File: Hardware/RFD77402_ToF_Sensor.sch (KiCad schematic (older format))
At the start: 18 parts, among them J1 QWIIC_CONNECTORJS-1MM, J2 QWIIC_CONNECTORJS-1MM, J3 CONN_01, J4 I2C_STANDARD, U1 RFD77402, U4 CC_LICENSE

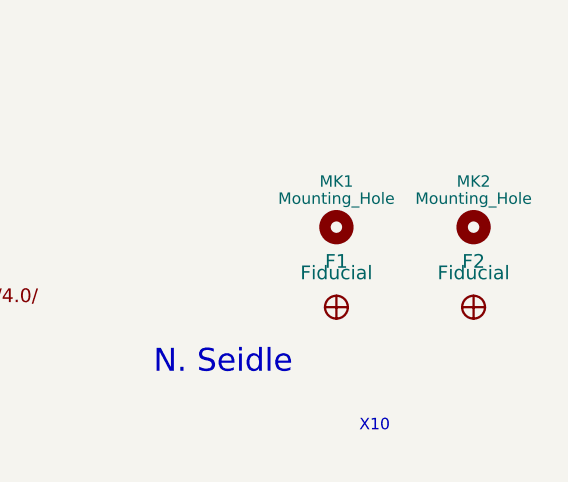
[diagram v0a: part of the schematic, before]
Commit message: Added fiducials
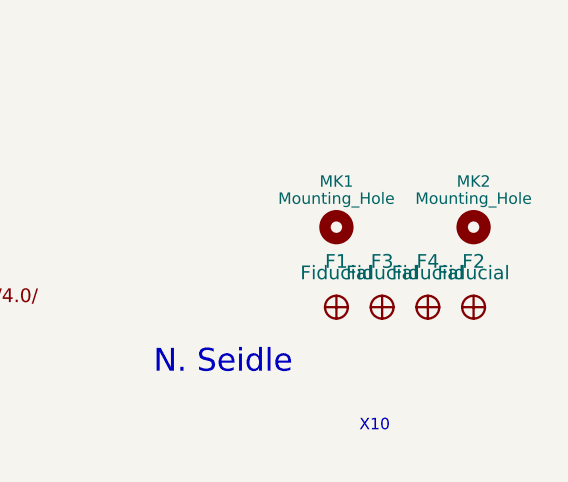
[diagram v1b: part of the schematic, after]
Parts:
- added F3, F4: Fiducial, Aesthetics:FIDUCIAL-MICRO, symbol Fiducial
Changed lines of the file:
@@
 $EndComp
 $Comp
-L GND #PWR01
+L GND #PWR8
 U 1 1 5907663F
 P 4650 5450
-F 0 "#PWR01" H 4650 5200 50  0001 C CNN
+F 0 "#PWR8" H 4650 5200 50  0001 C CNN
 F 1 "GND" H 4650 5300 50  0000 C CNN
 F 2 "" H 4650 5450 50  0001 C CNN
@@
 $EndComp
 $Comp
-L GND #PWR02
+L GND #PWR10
 U 1 1 5907732D
 P 4950 3200
-F 0 "#PWR02" H 4950 2950 50  0001 C CNN
+F 0 "#PWR10" H 4950 2950 50  0001 C CNN
 F 1 "GND" H 4950 3050 50  0000 C CNN
 F 2 "" H 4950 3200 50  0001 C CNN
@@
 $EndComp
 $Comp
-L GND #PWR03
+L GND #PWR4
 U 1 1 59077368
 P 4450 3200
-F 0 "#PWR03" H 4450 2950 50  0001 C CNN
+F 0 "#PWR4" H 4450 2950 50  0001 C CNN
 F 1 "GND" H 4450 3050 50  0000 C CNN
 F 2 "" H 4450 3200 50  0001 C CNN
@@
 $EndComp
 $Comp
-L +3.3V #PWR04
+L +3.3V #PWR3
 U 1 1 59078478
 P 4450 2650
-F 0 "#PWR04" H 4450 2500 50  0001 C CNN
+F 0 "#PWR3" H 4450 2500 50  0001 C CNN
 F 1 "+3.3V" H 4450 2790 50  0000 C CNN
 F 2 "" H 4450 2650 50  0001 C CNN
@@
 $EndComp
 $Comp
-L +3.3V #PWR05
+L +3.3V #PWR9
 U 1 1 590784B0
 P 4950 2700
-F 0 "#PWR05" H 4950 2550 50  0001 C CNN
+F 0 "#PWR9" H 4950 2550 50  0001 C CNN
 F 1 "+3.3V" H 4950 2840 50  0000 C CNN
 F 2 "" H 4950 2700 50  0001 C CNN
@@
 $EndComp
 $Comp
-L +3.3V #PWR06
+L +3.3V #PWR5
 U 1 1 590784E8
 P 4650 4000
-F 0 "#PWR06" H 4650 3850 50  0001 C CNN
+F 0 "#PWR5" H 4650 3850 50  0001 C CNN
 F 1 "+3.3V" H 4650 4140 50  0000 C CNN
 F 2 "" H 4650 4000 50  0001 C CNN
@@
 $EndComp
 $Comp
-L +3.3V #PWR07
+L +3.3V #PWR11
 U 1 1 59078610
 P 5850 4000
-F 0 "#PWR07" H 5850 3850 50  0001 C CNN
+F 0 "#PWR11" H 5850 3850 50  0001 C CNN
 F 1 "+3.3V" H 5850 4140 50  0000 C CNN
 F 2 "" H 5850 4000 50  0001 C CNN
@@
 $EndComp
 $Comp
-L +3.3V #PWR08
+L +3.3V #PWR7
 U 1 1 59078648
 P 4650 4950
-F 0 "#PWR08" H 4650 4800 50  0001 C CNN
+F 0 "#PWR7" H 4650 4800 50  0001 C CNN
 F 1 "+3.3V" H 4650 5090 50  0000 C CNN
 F 2 "" H 4650 4950 50  0001 C CNN
@@
 $EndComp
 $Comp
-L GND #PWR09
+L GND #PWR12
 U 1 1 590793B0
 P 5850 4500
-F 0 "#PWR09" H 5850 4250 50  0001 C CNN
+F 0 "#PWR12" H 5850 4250 50  0001 C CNN
 F 1 "GND" H 5850 4350 50  0000 C CNN
 F 2 "" H 5850 4500 50  0001 C CNN
@@
 $EndComp
 $Comp
-L GND #PWR010
+L GND #PWR6
 U 1 1 590795D3
 P 4650 4500
-F 0 "#PWR010" H 4650 4250 50  0001 C CNN
+F 0 "#PWR6" H 4650 4250 50  0001 C CNN
 F 1 "GND" H 4650 4350 50  0000 C CNN
 F 2 "" H 4650 4500 50  0001 C CNN
@@
 	5850 3100 5950 3100
 $Comp
-L +3.3V #PWR011
+L +3.3V #PWR13
 U 1 1 5907C92A
 P 6200 1950
-F 0 "#PWR011" H 6200 1800 50  0001 C CNN
+F 0 "#PWR13" H 6200 1800 50  0001 C CNN
 F 1 "+3.3V" H 6200 2090 50  0000 C CNN
 F 2 "" H 6200 1950 50  0001 C CNN
@@
 Connection ~ 4950 2800
 $Comp
-L +3.3V #PWR012
+L +3.3V #PWR1
 U 1 1 591D2B23
 P 4150 2650
-F 0 "#PWR012" H 4150 2500 50  0001 C CNN
+F 0 "#PWR1" H 4150 2500 50  0001 C CNN
 F 1 "+3.3V" H 4150 2790 50  0000 C CNN
 F 2 "" H 4150 2650 50  0001 C CNN
@@
 $EndComp
 $Comp
-L GND #PWR013
+L GND #PWR2
 U 1 1 591D2B5E
 P 4150 3200
-F 0 "#PWR013" H 4150 2950 50  0001 C CNN
+F 0 "#PWR2" H 4150 2950 50  0001 C CNN
 F 1 "GND" H 4150 3050 50  0000 C CNN
 F 2 "" H 4150 3200 50  0001 C CNN
@@
 	1    0    0    -1
 $EndComp
+$Comp
+L Fiducial F3
+U 1 1 5A0F19BD
+P 10000 7300
+F 0 "F3" H 10000 7500 60  0000 C CNN
+F 1 "Fiducial" H 10000 7450 60  0000 C CNN
+F 2 "Aesthetics:FIDUCIAL-MICRO" H 10000 7300 60  0001 C CNN
+F 3 "" H 10000 7300 60  0001 C CNN
+	1    10000 7300
+	1    0    0    -1
+$EndComp
+$Comp
+L Fiducial F4
+U 1 1 5A0F1A01
+P 10200 7300
+F 0 "F4" H 10200 7500 60  0000 C CNN
+F 1 "Fiducial" H 10200 7450 60  0000 C CNN
+F 2 "Aesthetics:FIDUCIAL-MICRO" H 10200 7300 60  0001 C CNN
+F 3 "" H 10200 7300 60  0001 C CNN
+	1    10200 7300
+	1    0    0    -1
+$EndComp

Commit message: Post design review changes
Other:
- note added: "Distance Sensor"
- note added: "I2C Address: 0X4C"
- note added: "I2C Connections"
- note added: "Jumper connects the I2C pullup resistors.\nDisconnect to use your own resistors."
- note added: "v01"
- note removed: "X10"
- moved on the sheet: F1, F2, F3, F4, MK1, MK2
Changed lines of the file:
@@
 N. Seidle
 Text Notes 9900 7850 0    50   ~ 0
-X10
-Wire Wire Line
-	5050 2800 4950 2800
-Wire Wire Line
-	4950 2700 4950 2900
-Wire Wire Line
-	4450 2650 4450 2800
-Wire Wire Line
-	4650 4300 4650 4000
-Wire Wire Line
-	5600 4300 5850 4300
-Wire Wire Line
-	5850 4300 5850 4000
-Wire Wire Line
-	4300 5250 4650 5250
-Wire Wire Line
-	4650 5250 4650 4950
-Wire Wire Line
-	5050 3100 4950 3100
-Wire Wire Line
-	4950 3000 4950 3200
-Wire Wire Line
-	4450 3100 4450 3200
-Wire Wire Line
-	4250 4400 4650 4400
-Wire Wire Line
-	4650 4400 4650 4500
-Wire Wire Line
-	5600 4400 5850 4400
-Wire Wire Line
-	5850 4400 5850 4500
-Wire Wire Line
-	4300 5350 4650 5350
-Wire Wire Line
-	4650 5350 4650 5450
-Wire Wire Line
-	6450 2250 6450 2300
-Wire Wire Line
-	6450 2250 6350 2250
-Wire Wire Line
-	5950 2250 5950 2300
-Wire Wire Line
-	5950 2250 6050 2250
-Wire Wire Line
-	5850 2800 6650 2800
-Wire Wire Line
-	5950 2700 5950 2800
-Connection ~ 5950 2800
-Wire Wire Line
-	4250 4100 4350 4100
-Wire Wire Line
-	5600 4100 5650 4100
-Wire Wire Line
-	4300 5050 4450 5050
-Wire Wire Line
-	5850 2900 6650 2900
-Wire Wire Line
-	6450 2700 6450 2900
-Connection ~ 6450 2900
-Wire Wire Line
-	4250 4200 4350 4200
-Wire Wire Line
-	5600 4200 5650 4200
-Wire Wire Line
-	4300 5150 4450 5150
-Wire Wire Line
-	5700 5100 5900 5100
+v01
 Text GLabel 5950 3100 2    39   Input ~ 0
 ~INT
@@
 L Mounting_Hole MK1
 U 1 1 59075789
-P 9800 6950
-F 0 "MK1" H 9800 7150 50  0000 C CNN
-F 1 "Mounting_Hole" H 9800 7075 50  0000 C CNN
-F 2 "SparkFun-Hardware:STAND-OFF" H 9800 6950 50  0001 C CNN
-F 3 "" H 9800 6950 50  0001 C CNN
-	1    9800 6950
+P 9600 6950
+F 0 "MK1" H 9600 7150 50  0000 C CNN
+F 1 "Mounting_Hole" H 9600 7075 50  0000 C CNN
+F 2 "SparkFun-Hardware:STAND-OFF" H 9600 6950 50  0001 C CNN
+F 3 "" H 9600 6950 50  0001 C CNN
+	1    9600 6950
 	1    0    0    -1
 $EndComp
@@
 	1    0    0    -1
 $EndComp
-Wire Wire Line
-	4250 4300 4650 4300
-Wire Wire Line
-	5850 3100 5950 3100
 $Comp
 L +3.3V #PWR13
@@
 	1    0    0    -1
 $EndComp
-Wire Wire Line
-	6200 1950 6200 2100
 $Comp
 L JUMPER-SMT_3_2-NC_PASTE_SILK JP1
@@
 L Mounting_Hole MK2
 U 1 1 59084A42
-P 10400 6950
-F 0 "MK2" H 10400 7150 50  0000 C CNN
-F 1 "Mounting_Hole" H 10400 7075 50  0000 C CNN
-F 2 "SparkFun-Hardware:STAND-OFF" H 10400 6950 50  0001 C CNN
-F 3 "" H 10400 6950 50  0001 C CNN
-	1    10400 6950
+P 10200 6950
+F 0 "MK2" H 10200 7150 50  0000 C CNN
+F 1 "Mounting_Hole" H 10200 7075 50  0000 C CNN
+F 2 "SparkFun-Hardware:STAND-OFF" H 10200 6950 50  0001 C CNN
+F 3 "" H 10200 6950 50  0001 C CNN
+	1    10200 6950
 	1    0    0    -1
 $EndComp
@@
 L Fiducial F2
 U 1 1 59092D95
-P 10400 7300
-F 0 "F2" H 10400 7500 60  0000 C CNN
-F 1 "Fiducial" H 10400 7450 60  0000 C CNN
-F 2 "Aesthetics:FIDUCIAL-MICRO" H 10400 7300 60  0001 C CNN
-F 3 "" H 10400 7300 60  0001 C CNN
-	1    10400 7300
+P 10250 7250
+F 0 "F2" H 10250 7450 60  0000 C CNN
+F 1 "Fiducial" H 10250 7400 60  0000 C CNN
+F 2 "Aesthetics:FIDUCIAL-MICRO" H 10250 7250 60  0001 C CNN
+F 3 "" H 10250 7250 60  0001 C CNN
+	1    10250 7250
 	1    0    0    -1
 $EndComp
@@
 L Fiducial F1
 U 1 1 59092EBB
-P 9800 7300
-F 0 "F1" H 9800 7500 60  0000 C CNN
-F 1 "Fiducial" H 9800 7450 60  0000 C CNN
-F 2 "Aesthetics:FIDUCIAL-MICRO" H 9800 7300 60  0001 C CNN
-F 3 "" H 9800 7300 60  0001 C CNN
-	1    9800 7300
-	1    0    0    -1
-$EndComp
-Wire Wire Line
-	5050 3000 4950 3000
-Connection ~ 4950 3100
-Wire Wire Line
-	4950 2900 5050 2900
-Connection ~ 4950 2800
+P 9600 7250
+F 0 "F1" H 9600 7450 60  0000 C CNN
+F 1 "Fiducial" H 9600 7400 60  0000 C CNN
+F 2 "Aesthetics:FIDUCIAL-MICRO" H 9600 7250 60  0001 C CNN
+F 3 "" H 9600 7250 60  0001 C CNN
+	1    9600 7250
+	1    0    0    -1
+$EndComp
 $Comp
 L +3.3V #PWR1
@@
 	1    0    0    -1
 $EndComp
-Wire Wire Line
-	4150 3100 4150 3200
-Wire Wire Line
-	4150 2650 4150 2800
 $Comp
 L I2C_STANDARD J4
@@
 L Fiducial F3
 U 1 1 5A0F19BD
-P 10000 7300
-F 0 "F3" H 10000 7500 60  0000 C CNN
-F 1 "Fiducial" H 10000 7450 60  0000 C CNN
-F 2 "Aesthetics:FIDUCIAL-MICRO" H 10000 7300 60  0001 C CNN
-F 3 "" H 10000 7300 60  0001 C CNN
-	1    10000 7300
+P 9800 7250
+F 0 "F3" H 9800 7450 60  0000 C CNN
+F 1 "Fiducial" H 9800 7400 60  0000 C CNN
+F 2 "Aesthetics:FIDUCIAL-MICRO" H 9800 7250 60  0001 C CNN
+F 3 "" H 9800 7250 60  0001 C CNN
+	1    9800 7250
 	1    0    0    -1
 $EndComp
@@
 L Fiducial F4
 U 1 1 5A0F1A01
-P 10200 7300
-F 0 "F4" H 10200 7500 60  0000 C CNN
-F 1 "Fiducial" H 10200 7450 60  0000 C CNN
-F 2 "Aesthetics:FIDUCIAL-MICRO" H 10200 7300 60  0001 C CNN
-F 3 "" H 10200 7300 60  0001 C CNN
-	1    10200 7300
-	1    0    0    -1
-$EndComp
+P 10000 7250
+F 0 "F4" H 10000 7450 60  0000 C CNN
+F 1 "Fiducial" H 10000 7400 60  0000 C CNN
+F 2 "Aesthetics:FIDUCIAL-MICRO" H 10000 7250 60  0001 C CNN
+F 3 "" H 10000 7250 60  0001 C CNN
+	1    10000 7250
+	1    0    0    -1
+$EndComp
+Wire Wire Line
+	5050 2800 4950 2800
+Wire Wire Line
+	4950 2700 4950 2900
+Wire Wire Line
+	4450 2650 4450 2800
+Wire Wire Line
+	4650 4300 4650 4000
+Wire Wire Line
+	5600 4300 5850 4300
+Wire Wire Line
+	5850 4300 5850 4000
+Wire Wire Line
+	4300 5250 4650 5250
+Wire Wire Line
+	4650 5250 4650 4950
+Wire Wire Line
+	5050 3100 4950 3100
+Wire Wire Line
+	4950 3000 4950 3200
+Wire Wire Line
+	4450 3100 4450 3200
+Wire Wire Line
+	4250 4400 4650 4400
+Wire Wire Line
+	4650 4400 4650 4500
+Wire Wire Line
+	5600 4400 5850 4400
+Wire Wire Line
+	5850 4400 5850 4500
+Wire Wire Line
+	4300 5350 4650 5350
+Wire Wire Line
+	4650 5350 4650 5450
+Wire Wire Line
+	6450 2250 6450 2300
+Wire Wire Line
+	6450 2250 6350 2250
+Wire Wire Line
+	5950 2250 5950 2300
+Wire Wire Line
+	5950 2250 6050 2250
+Wire Wire Line
+	5850 2800 6650 2800
+Wire Wire Line
+	5950 2700 5950 2800
+Connection ~ 5950 2800
+Wire Wire Line
+	4250 4100 4350 4100
+Wire Wire Line
+	5600 4100 5650 4100
+Wire Wire Line
+	4300 5050 4450 5050
+Wire Wire Line
+	5850 2900 6650 2900
+Wire Wire Line
+	6450 2700 6450 2900
+Connection ~ 6450 2900
+Wire Wire Line
+	4250 4200 4350 4200
+Wire Wire Line
+	5600 4200 5650 4200
+Wire Wire Line
+	4300 5150 4450 5150
+Wire Wire Line
+	5700 5100 5900 5100
+Wire Wire Line
+	4250 4300 4650 4300
+Wire Wire Line
+	5850 3100 5950 3100
+Wire Wire Line
+	6200 1950 6200 2100
+Wire Wire Line
+	5050 3000 4950 3000
+Connection ~ 4950 3100
+Wire Wire Line
+	4950 2900 5050 2900
+Connection ~ 4950 2800
+Wire Wire Line
+	4150 3100 4150 3200
+Wire Wire Line
+	4150 2650 4150 2800
+Wire Notes Line
+	500  3500 10550 3500
+Wire Notes Line
+	10550 3500 10550 3450
+Text Notes 4950 1500 0    60   ~ 0
+Distance Sensor
+Text Notes 4650 3650 0    60   ~ 0
+I2C Connections
+Text Notes 6500 1800 0    60   ~ 0
+Jumper connects the I2C pullup resistors.\nDisconnect to use your own resistors.
+Text Notes 5050 3450 0    60   ~ 0
+I2C Address: 0X4C
 $EndSCHEMATC

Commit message: post design review changes
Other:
- note added: "Designed by: N. Seidle\n"
- note added: "Revised by: A. England"
- note added: "v10"
- note removed: "N. Seidle"
- note removed: "v01"
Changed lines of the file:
@@
 Comment4 ""
 $EndDescr
-Text Notes 9000 7600 0    100  ~ 0
-N. Seidle
 Text Notes 9900 7850 0    50   ~ 0
-v01
+v10
 Text GLabel 5950 3100 2    39   Input ~ 0
 ~INT
@@
 $EndComp
 $Comp
-L GND #PWR8
+L GND #PWR01
 U 1 1 5907663F
 P 4650 5450
-F 0 "#PWR8" H 4650 5200 50  0001 C CNN
+F 0 "#PWR01" H 4650 5200 50  0001 C CNN
 F 1 "GND" H 4650 5300 50  0000 C CNN
 F 2 "" H 4650 5450 50  0001 C CNN
@@
 $EndComp
 $Comp
-L GND #PWR10
+L GND #PWR02
 U 1 1 5907732D
 P 4950 3200
-F 0 "#PWR10" H 4950 2950 50  0001 C CNN
+F 0 "#PWR02" H 4950 2950 50  0001 C CNN
 F 1 "GND" H 4950 3050 50  0000 C CNN
 F 2 "" H 4950 3200 50  0001 C CNN
@@
 $EndComp
 $Comp
-L GND #PWR4
+L GND #PWR03
 U 1 1 59077368
 P 4450 3200
-F 0 "#PWR4" H 4450 2950 50  0001 C CNN
+F 0 "#PWR03" H 4450 2950 50  0001 C CNN
 F 1 "GND" H 4450 3050 50  0000 C CNN
 F 2 "" H 4450 3200 50  0001 C CNN
@@
 $EndComp
 $Comp
-L +3.3V #PWR3
+L +3.3V #PWR04
 U 1 1 59078478
 P 4450 2650
-F 0 "#PWR3" H 4450 2500 50  0001 C CNN
+F 0 "#PWR04" H 4450 2500 50  0001 C CNN
 F 1 "+3.3V" H 4450 2790 50  0000 C CNN
 F 2 "" H 4450 2650 50  0001 C CNN
@@
 $EndComp
 $Comp
-L +3.3V #PWR9
+L +3.3V #PWR05
 U 1 1 590784B0
 P 4950 2700
-F 0 "#PWR9" H 4950 2550 50  0001 C CNN
+F 0 "#PWR05" H 4950 2550 50  0001 C CNN
 F 1 "+3.3V" H 4950 2840 50  0000 C CNN
 F 2 "" H 4950 2700 50  0001 C CNN
@@
 $EndComp
 $Comp
-L +3.3V #PWR5
+L +3.3V #PWR06
 U 1 1 590784E8
 P 4650 4000
-F 0 "#PWR5" H 4650 3850 50  0001 C CNN
+F 0 "#PWR06" H 4650 3850 50  0001 C CNN
 F 1 "+3.3V" H 4650 4140 50  0000 C CNN
 F 2 "" H 4650 4000 50  0001 C CNN
@@
 $EndComp
 $Comp
-L +3.3V #PWR11
+L +3.3V #PWR07
 U 1 1 59078610
 P 5850 4000
-F 0 "#PWR11" H 5850 3850 50  0001 C CNN
+F 0 "#PWR07" H 5850 3850 50  0001 C CNN
 F 1 "+3.3V" H 5850 4140 50  0000 C CNN
 F 2 "" H 5850 4000 50  0001 C CNN
@@
 $EndComp
 $Comp
-L +3.3V #PWR7
+L +3.3V #PWR08
 U 1 1 59078648
 P 4650 4950
-F 0 "#PWR7" H 4650 4800 50  0001 C CNN
+F 0 "#PWR08" H 4650 4800 50  0001 C CNN
 F 1 "+3.3V" H 4650 5090 50  0000 C CNN
 F 2 "" H 4650 4950 50  0001 C CNN
@@
 $EndComp
 $Comp
-L GND #PWR12
+L GND #PWR09
 U 1 1 590793B0
 P 5850 4500
-F 0 "#PWR12" H 5850 4250 50  0001 C CNN
+F 0 "#PWR09" H 5850 4250 50  0001 C CNN
 F 1 "GND" H 5850 4350 50  0000 C CNN
 F 2 "" H 5850 4500 50  0001 C CNN
@@
 $EndComp
 $Comp
-L GND #PWR6
+L GND #PWR010
 U 1 1 590795D3
 P 4650 4500
-F 0 "#PWR6" H 4650 4250 50  0001 C CNN
+F 0 "#PWR010" H 4650 4250 50  0001 C CNN
 F 1 "GND" H 4650 4350 50  0000 C CNN
 F 2 "" H 4650 4500 50  0001 C CNN
@@
 $EndComp
 $Comp
-L +3.3V #PWR13
+L +3.3V #PWR011
 U 1 1 5907C92A
 P 6200 1950
-F 0 "#PWR13" H 6200 1800 50  0001 C CNN
+F 0 "#PWR011" H 6200 1800 50  0001 C CNN
 F 1 "+3.3V" H 6200 2090 50  0000 C CNN
 F 2 "" H 6200 1950 50  0001 C CNN
@@
 $EndComp
 $Comp
-L +3.3V #PWR1
+L +3.3V #PWR012
 U 1 1 591D2B23
 P 4150 2650
-F 0 "#PWR1" H 4150 2500 50  0001 C CNN
+F 0 "#PWR012" H 4150 2500 50  0001 C CNN
 F 1 "+3.3V" H 4150 2790 50  0000 C CNN
 F 2 "" H 4150 2650 50  0001 C CNN
@@
 $EndComp
 $Comp
-L GND #PWR2
+L GND #PWR013
 U 1 1 591D2B5E
 P 4150 3200
-F 0 "#PWR2" H 4150 2950 50  0001 C CNN
+F 0 "#PWR013" H 4150 2950 50  0001 C CNN
 F 1 "GND" H 4150 3050 50  0000 C CNN
 F 2 "" H 4150 3200 50  0001 C CNN
@@
 Text Notes 5050 3450 0    60   ~ 0
 I2C Address: 0X4C
+Text Notes 7850 7600 0    60   ~ 0
+Designed by: N. Seidle\n
+Text Notes 9200 7600 0    60   ~ 0
+Revised by: A. England
 $EndSCHEMATC

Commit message: fixed paste issue with fiducial
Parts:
- F1, F2, F3, F4: footprint Aesthetics:FIDUCIAL-MICRO -> Aesthetics:FIDUCIAL-MICRO-NO_PASTE
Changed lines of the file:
@@
-$EndComp
-$Comp
-L Fiducial F2
-U 1 1 59092D95
-P 10250 7250
-F 0 "F2" H 10250 7450 60  0000 C CNN
-F 1 "Fiducial" H 10250 7400 60  0000 C CNN
-F 2 "Aesthetics:FIDUCIAL-MICRO" H 10250 7250 60  0001 C CNN
-F 3 "" H 10250 7250 60  0001 C CNN
-	1    10250 7250
-	1    0    0    -1
-$EndComp
-$Comp
-L Fiducial F1
-U 1 1 59092EBB
-P 9600 7250
-F 0 "F1" H 9600 7450 60  0000 C CNN
-F 1 "Fiducial" H 9600 7400 60  0000 C CNN
-F 2 "Aesthetics:FIDUCIAL-MICRO" H 9600 7250 60  0001 C CNN
-F 3 "" H 9600 7250 60  0001 C CNN
-	1    9600 7250
-	1    0    0    -1
 $EndComp
 $Comp
@@
 F 4 "XXX-00000" H 4300 8550 60  0000 C CNN "Field4"
 	1    4000 8000
-	1    0    0    -1
-$EndComp
-$Comp
-L Fiducial F3
-U 1 1 5A0F19BD
-P 9800 7250
-F 0 "F3" H 9800 7450 60  0000 C CNN
-F 1 "Fiducial" H 9800 7400 60  0000 C CNN
-F 2 "Aesthetics:FIDUCIAL-MICRO" H 9800 7250 60  0001 C CNN
-F 3 "" H 9800 7250 60  0001 C CNN
-	1    9800 7250
-	1    0    0    -1
-$EndComp
-$Comp
-L Fiducial F4
-U 1 1 5A0F1A01
-P 10000 7250
-F 0 "F4" H 10000 7450 60  0000 C CNN
-F 1 "Fiducial" H 10000 7400 60  0000 C CNN
-F 2 "Aesthetics:FIDUCIAL-MICRO" H 10000 7250 60  0001 C CNN
-F 3 "" H 10000 7250 60  0001 C CNN
-	1    10000 7250
 	1    0    0    -1
 $EndComp
@@
 Text Notes 9200 7600 0    60   ~ 0
 Revised by: A. England
+$Comp
+L Fiducial F2
+U 1 1 59092D95
+P 10250 7250
+F 0 "F2" H 10250 7450 60  0000 C CNN
+F 1 "Fiducial" H 10250 7400 60  0000 C CNN
+F 2 "Aesthetics:FIDUCIAL-MICRO-NO_PASTE" H 10250 7250 60  0001 C CNN
+F 3 "" H 10250 7250 60  0001 C CNN
+	1    10250 7250
+	1    0    0    -1
+$EndComp
+$Comp
+L Fiducial F4
+U 1 1 5A0F1A01
+P 10000 7250
+F 0 "F4" H 10000 7450 60  0000 C CNN
+F 1 "Fiducial" H 10000 7400 60  0000 C CNN
+F 2 "Aesthetics:FIDUCIAL-MICRO-NO_PASTE" H 10000 7250 60  0001 C CNN
+F 3 "" H 10000 7250 60  0001 C CNN
+	1    10000 7250
+	1    0    0    -1
+$EndComp
+$Comp
+L Fiducial F3
+U 1 1 5A0F19BD
+P 9800 7250
+F 0 "F3" H 9800 7450 60  0000 C CNN
+F 1 "Fiducial" H 9800 7400 60  0000 C CNN
+F 2 "Aesthetics:FIDUCIAL-MICRO-NO_PASTE" H 9800 7250 60  0001 C CNN
+F 3 "" H 9800 7250 60  0001 C CNN
+	1    9800 7250
+	1    0    0    -1
+$EndComp
+$Comp
+L Fiducial F1
+U 1 1 59092EBB
+P 9600 7250
+F 0 "F1" H 9600 7450 60  0000 C CNN
+F 1 "Fiducial" H 9600 7400 60  0000 C CNN
+F 2 "Aesthetics:FIDUCIAL-MICRO-NO_PASTE" H 9600 7250 60  0001 C CNN
+F 3 "" H 9600 7250 60  0001 C CNN
+	1    9600 7250
+	1    0    0    -1
+$EndComp
 $EndSCHEMATC
